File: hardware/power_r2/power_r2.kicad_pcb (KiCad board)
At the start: 2 copper layers, 131.5 x 12.9 mm, 53 parts, among them J101 FPC Connector, J102 Power Input, Q101 AONR21357, U101 SIC473

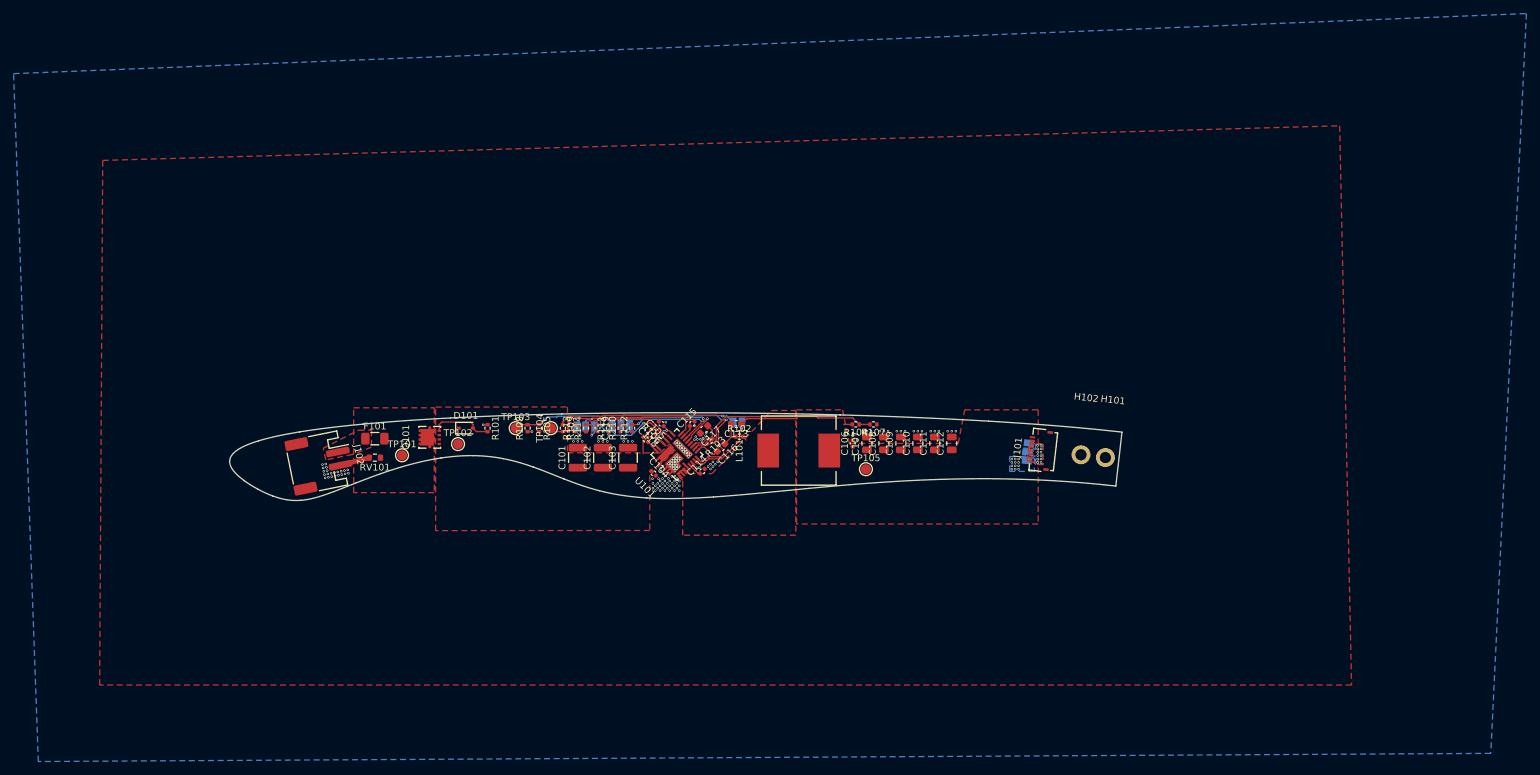
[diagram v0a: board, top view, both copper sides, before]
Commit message: Next revision of the boards are finished and ready for fabrication, and a BOM has been added.
The BOM is still missing components for the nucleo shield.
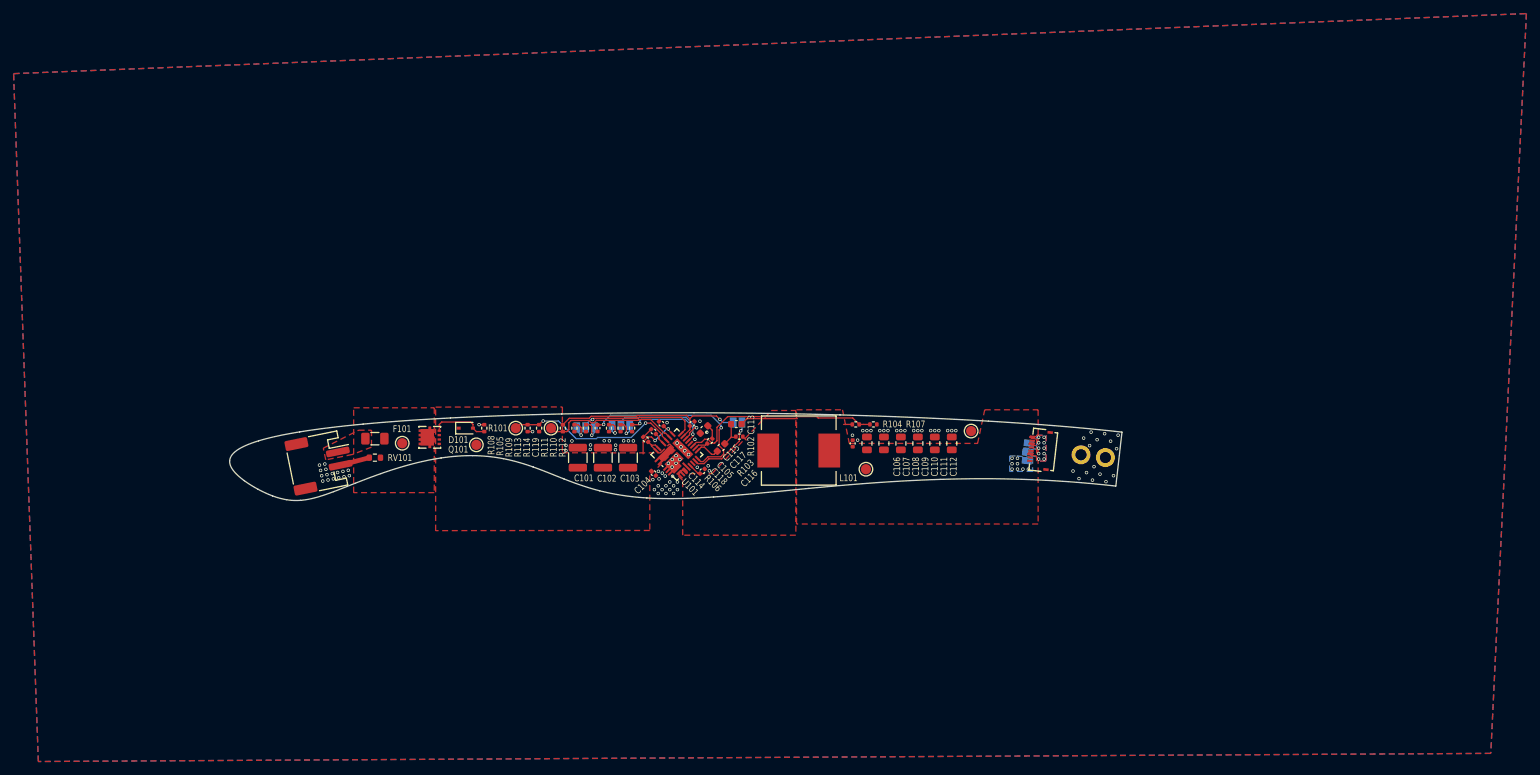
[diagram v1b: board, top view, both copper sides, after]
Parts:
- added G***: LOGO, rave_shades:logo_size_1, B.Cu at (156.2, 107.0)
- added TP106: GND Test Point, TestPoint:TestPoint_Pad_D1.5mm, F.Cu at (178.2, 102.9)
- C106, C119: value 100n -> 100n 100V
- C118: value 100n 50V -> 100n 100V
- JP101, JP102, JP103: footprint Jumper:SolderJumper-3_P1.3mm_Open_Pad1.0x1.5mm -> rave_shades:SolderJumper-3_P1.3mm_Open_Pad1.0x1.5mm
- R101, R109, R114: value 10k -> 10k 1%
- moved TP102 2.70 mm to (105.3, 104.9)
- moved TP101 1.78 mm to (94.4, 104.7)
- moved R101 0.48 mm to (106.5, 102.5)
- moved JP103 0.14 mm to (121.4, 102.3)
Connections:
- J101 pad 1: /+5V_OR_GND -> /SPARE_1_5V0
- J101 pad 2: +5V -> /SPARE_0_5V0
- J101 pad 3: /+5V_OR_GND -> /5V0_OR_GND
- J101 pad 6: /+5V_OR_GND -> /5V0_OR_GND
- J101 pad 7: /SPARE_0_5V0 -> +5V
- J101 pad 8: /SPARE_1_5V0 -> /5V0_OR_GND
- JP101 pad 2: /+5V_OR_GND -> /5V0_OR_GND
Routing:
- net /F_SW: track 16.2 -> 12.4 mm
- net /I_LIMIT: track 17.1 -> 15.0 mm
- net /SS: track 30.4 -> 28.8 mm
- net /EN: track 26.7 -> 25.9 mm
- net /V_SAFE: track 8.11 -> 8.64 mm
- net GND: track 5.68 -> 5.88 mm, vias 154 -> 101
- net /5V0_OR_GND: vias 0 -> 10
- net /+5V_OR_GND: vias 12 -> 0
- net +5V: vias 12 -> 8
- added copper zone on B.Cu, net /5V0_OR_GND
- added copper zone on F.Cu, net /5V0_OR_GND
- added copper zone on In1.Cu, net GND
- added copper zone on In2.Cu, net GND
- removed copper zone on B.Cu, net /+5V_OR_GND
- removed copper zone on F.Cu, net /+5V_OR_GND
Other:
- copper layers 2 -> 4
- board text added: "1.5A"
- board text added: "1.5A 3A"
- board text added: "3A"
- board text added: "CURRENT LIMIT"
- board text added: "EFFICIENT SWITCHING"
- board text added: "ENABLED DISABLED"
- board text added: "POWER REV 2"
- board text added: "ULTRASONIC ENABLE"

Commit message: Updated kicad files to work with latest kicad. Added some todos for next hw design.
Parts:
- D101: value ESDA17P20-1F2 -> D5V0L1B2WS-7
